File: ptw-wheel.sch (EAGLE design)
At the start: 3 parts

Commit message: Create board data
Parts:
- removed ARDUINO_NANO3: Arduino Nano, ArduinoNanoV30:ARDUINO_NANO
- removed KNS1: KONASHI-2.0, konashi-2.0:KONASHI-2.0
- added ARDUINO_NANO1: (no value), arduinoNanoV30-withoud_drill_hole:ARDUINO_NANO
- added U$1: KONASHI2.0, konashiv2-withoud_drill_hole:KONASHI2.0
- added USB1: USBCON, usbcon:USBCON
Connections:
- removed net N$2: ARDUINO_NANO3.GND@2, JP1.3
- removed net N$6: ARDUINO_NANO3.GND@1, KNS1.UART-GND
- new net +5V: ARDUINO_NANO1.5V, JP1.1, U$1.+5V, USB1.5V
- new net GND: ARDUINO_NANO1.GND@1, JP1.3, U$1.GND, U$1.GND@1, U$1.GND@2, USB1.GND, USB1.SHIELD
- net N$1: now also ARDUINO_NANO1.GND@2, U$1.GND@3; no longer ARDUINO_NANO3.5V, JP1.1, KNS1.+5V
- net N$3: now also ARDUINO_NANO1.D6/AIN0; no longer ARDUINO_NANO3.D6/AIN0
- net N$4: now also ARDUINO_NANO1.D0/RX, U$1.TX; no longer ARDUINO_NANO3.D0/RX, KNS1.UART-TX
- net N$5: now also ARDUINO_NANO1.D1/TX, U$1.RX; no longer ARDUINO_NANO3.D1/TX, KNS1.UART-RX
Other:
- moved on the sheet: JP1

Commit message: Rename connection to 'GND'
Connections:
- removed net N$1: ARDUINO_NANO1.GND@2, U$1.GND@3
- net GND: now also ARDUINO_NANO1.GND@2, U$1.GND@3
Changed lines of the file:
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@@
 <pinref part="U$1" gate="G$1" pin="GND"/>
+</segment>
+<segment>
+<pinref part="ARDUINO_NANO1" gate="G$1" pin="GND@2"/>
+<wire x1="48.26" y1="53.34" x2="53.34" y2="53.34" width="0.1524" layer="91"/>
+<pinref part="SUPPLY5" gate="GND" pin="GND"/>
+<wire x1="53.34" y1="53.34" x2="53.34" y2="40.64" width="0.1524" layer="91"/>
+<pinref part="U$1" gate="G$1" pin="GND@3"/>
+<wire x1="60.96" y1="40.64" x2="53.34" y2="40.64" width="0.1524" layer="91"/>
+<junction x="53.34" y="40.64"/>
 </segment>
 </net>
@@
 </segment>
 </net>
-<net name="N$1" class="0">
-<segment>
-<pinref part="ARDUINO_NANO1" gate="G$1" pin="GND@2"/>
-<wire x1="48.26" y1="53.34" x2="53.34" y2="53.34" width="0.1524" layer="91"/>
-<pinref part="SUPPLY5" gate="GND" pin="GND"/>
-<wire x1="53.34" y1="53.34" x2="53.34" y2="40.64" width="0.1524" layer="91"/>
-<wire x1="60.96" y1="40.64" x2="53.34" y2="40.64" width="0.1524" layer="91"/>
-<junction x="53.34" y="40.64"/>
-<pinref part="U$1" gate="G$1" pin="GND@3"/>
-</segment>
-</net>

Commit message: 更新
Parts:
- renumbered U$1 to KONASHI
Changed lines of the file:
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@@
 <part name="SUPPLY8" library="supply2" library_urn="urn:adsk.eagle:library:372" deviceset="GND" device=""/>
 <part name="SUPPLY10" library="supply2" library_urn="urn:adsk.eagle:library:372" deviceset="GND" device=""/>
-<part name="U$1" library="konashiv2-withoud_drill_hole" deviceset="KONASHI2.0" device=""/>
+<part name="KONASHI" library="konashiv2-withoud_drill_hole" deviceset="KONASHI2.0" device=""/>
 </parts>
 <sheets>
@@
 <attribute name="VALUE" x="104.775" y="14.605" size="1.778" layer="96"/>
 </instance>
-<instance part="U$1" gate="G$1" x="83.82" y="33.02" smashed="yes" rot="R90"/>
+<instance part="KONASHI" gate="G$1" x="83.82" y="33.02" smashed="yes" rot="R90"/>
 </instances>
 <busses>
@@
 <wire x1="58.42" y1="43.18" x2="60.96" y2="43.18" width="0.1524" layer="91"/>
 <pinref part="ARDUINO_NANO1" gate="G$1" pin="D0/RX"/>
-<pinref part="U$1" gate="G$1" pin="TX"/>
+<pinref part="KONASHI" gate="G$1" pin="TX"/>
 </segment>
 </net>
@@
 <wire x1="55.88" y1="38.1" x2="60.96" y2="38.1" width="0.1524" layer="91"/>
 <pinref part="ARDUINO_NANO1" gate="G$1" pin="D1/TX"/>
-<pinref part="U$1" gate="G$1" pin="RX"/>
+<pinref part="KONASHI" gate="G$1" pin="RX"/>
 </segment>
 </net>
@@
 <wire x1="106.68" y1="35.56" x2="111.76" y2="35.56" width="0.1524" layer="91"/>
 <pinref part="SUPPLY2" gate="GND" pin="GND"/>
-<pinref part="U$1" gate="G$1" pin="GND@1"/>
+<pinref part="KONASHI" gate="G$1" pin="GND@1"/>
 </segment>
 <segment>
@@
 <segment>
 <pinref part="SUPPLY8" gate="GND" pin="GND"/>
-<pinref part="U$1" gate="G$1" pin="GND@2"/>
+<pinref part="KONASHI" gate="G$1" pin="GND@2"/>
 </segment>
 <segment>
 <pinref part="SUPPLY10" gate="GND" pin="GND"/>
-<pinref part="U$1" gate="G$1" pin="GND"/>
+<pinref part="KONASHI" gate="G$1" pin="GND"/>
 </segment>
 <segment>
@@
 <pinref part="SUPPLY5" gate="GND" pin="GND"/>
 <wire x1="53.34" y1="53.34" x2="53.34" y2="40.64" width="0.1524" layer="91"/>
-<pinref part="U$1" gate="G$1" pin="GND@3"/>
+<pinref part="KONASHI" gate="G$1" pin="GND@3"/>
 <wire x1="60.96" y1="40.64" x2="53.34" y2="40.64" width="0.1524" layer="91"/>
 <junction x="53.34" y="40.64"/>
@@
 <pinref part="SUPPLY9" gate="+5V" pin="+5V"/>
 <junction x="111.76" y="40.64"/>
-<pinref part="U$1" gate="G$1" pin="+5V"/>
+<pinref part="KONASHI" gate="G$1" pin="+5V"/>
 </segment>
 <segment>

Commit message: ボードのレイアウト整理
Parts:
- renumbered ARDUINO_NANO1 to ARDUINO_NANO, USB1 to USB
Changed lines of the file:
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@@
 <parts>
 <part name="JP1" library="pinhead" library_urn="urn:adsk.eagle:library:325" deviceset="PINHD-1X3" device="" package3d_urn="urn:adsk.eagle:package:22458/2" value="LED tapes"/>
-<part name="USB1" library="usbcon" deviceset="USBCON" device=""/>
-<part name="ARDUINO_NANO1" library="arduinoNanoV30-withoud_drill_hole" deviceset="ARDUINO_NANO" device=""/>
+<part name="USB" library="usbcon" deviceset="USBCON" device=""/>
+<part name="ARDUINO_NANO" library="arduinoNanoV30-withoud_drill_hole" deviceset="ARDUINO_NANO" device=""/>
 <part name="SUPPLY1" library="supply2" library_urn="urn:adsk.eagle:library:372" deviceset="GND" device=""/>
 <part name="SUPPLY2" library="supply2" library_urn="urn:adsk.eagle:library:372" deviceset="GND" device=""/>
@@
 <attribute name="VALUE" x="129.54" y="57.15" size="1.778" layer="96" rot="R180"/>
 </instance>
-<instance part="USB1" gate="G$1" x="83.82" y="60.96" smashed="yes">
+<instance part="USB" gate="G$1" x="83.82" y="60.96" smashed="yes">
 <attribute name="NAME" x="78.74" y="68.58" size="1.778" layer="95"/>
 <attribute name="VALUE" x="78.74" y="50.8" size="1.778" layer="96"/>
 </instance>
-<instance part="ARDUINO_NANO1" gate="G$1" x="27.94" y="33.02" smashed="yes">
+<instance part="ARDUINO_NANO" gate="G$1" x="27.94" y="33.02" smashed="yes">
 <attribute name="NAME" x="12.7" y="12.7" size="1.778" layer="95"/>
 <attribute name="VALUE" x="12.7" y="10.16" size="1.778" layer="96"/>
@@
 <wire x1="7.62" y1="35.56" x2="5.08" y2="35.56" width="0.1524" layer="91"/>
 <wire x1="5.08" y1="35.56" x2="5.08" y2="7.62" width="0.1524" layer="91"/>
-<pinref part="ARDUINO_NANO1" gate="G$1" pin="D6/AIN0"/>
+<pinref part="ARDUINO_NANO" gate="G$1" pin="D6/AIN0"/>
 </segment>
 </net>
@@
 <wire x1="58.42" y1="63.5" x2="58.42" y2="43.18" width="0.1524" layer="91"/>
 <wire x1="58.42" y1="43.18" x2="60.96" y2="43.18" width="0.1524" layer="91"/>
-<pinref part="ARDUINO_NANO1" gate="G$1" pin="D0/RX"/>
+<pinref part="ARDUINO_NANO" gate="G$1" pin="D0/RX"/>
 <pinref part="KONASHI" gate="G$1" pin="TX"/>
 </segment>
@@
 <wire x1="55.88" y1="66.04" x2="55.88" y2="38.1" width="0.1524" layer="91"/>
 <wire x1="55.88" y1="38.1" x2="60.96" y2="38.1" width="0.1524" layer="91"/>
-<pinref part="ARDUINO_NANO1" gate="G$1" pin="D1/TX"/>
+<pinref part="ARDUINO_NANO" gate="G$1" pin="D1/TX"/>
 <pinref part="KONASHI" gate="G$1" pin="RX"/>
 </segment>
@@
 <net name="GND" class="0">
 <segment>
-<pinref part="USB1" gate="G$1" pin="GND"/>
+<pinref part="USB" gate="G$1" pin="GND"/>
 <wire x1="83.82" y1="60.96" x2="73.66" y2="60.96" width="0.1524" layer="91"/>
 <wire x1="73.66" y1="60.96" x2="73.66" y2="58.42" width="0.1524" layer="91"/>
-<pinref part="USB1" gate="G$1" pin="SHIELD"/>
+<pinref part="USB" gate="G$1" pin="SHIELD"/>
 <wire x1="83.82" y1="58.42" x2="73.66" y2="58.42" width="0.1524" layer="91"/>
 <junction x="73.66" y="58.42"/>
@@
 </segment>
 <segment>
-<pinref part="ARDUINO_NANO1" gate="G$1" pin="GND@1"/>
+<pinref part="ARDUINO_NANO" gate="G$1" pin="GND@1"/>
 <pinref part="SUPPLY4" gate="GND" pin="GND"/>
 <wire x1="2.54" y1="48.26" x2="7.62" y2="48.26" width="0.1524" layer="91"/>
@@
 </segment>
 <segment>
-<pinref part="ARDUINO_NANO1" gate="G$1" pin="GND@2"/>
+<pinref part="ARDUINO_NANO" gate="G$1" pin="GND@2"/>
 <wire x1="48.26" y1="53.34" x2="53.34" y2="53.34" width="0.1524" layer="91"/>
 <pinref part="SUPPLY5" gate="GND" pin="GND"/>
@@
 <net name="+5V" class="0">
 <segment>
-<pinref part="USB1" gate="G$1" pin="5V"/>
+<pinref part="USB" gate="G$1" pin="5V"/>
 <wire x1="83.82" y1="63.5" x2="73.66" y2="63.5" width="0.1524" layer="91"/>
 <pinref part="SUPPLY6" gate="+5V" pin="+5V"/>
@@
 <segment>
 <wire x1="48.26" y1="48.26" x2="50.8" y2="48.26" width="0.1524" layer="91"/>
-<pinref part="ARDUINO_NANO1" gate="G$1" pin="5V"/>
+<pinref part="ARDUINO_NANO" gate="G$1" pin="5V"/>
 <pinref part="SUPPLY7" gate="+5V" pin="+5V"/>
 </segment>

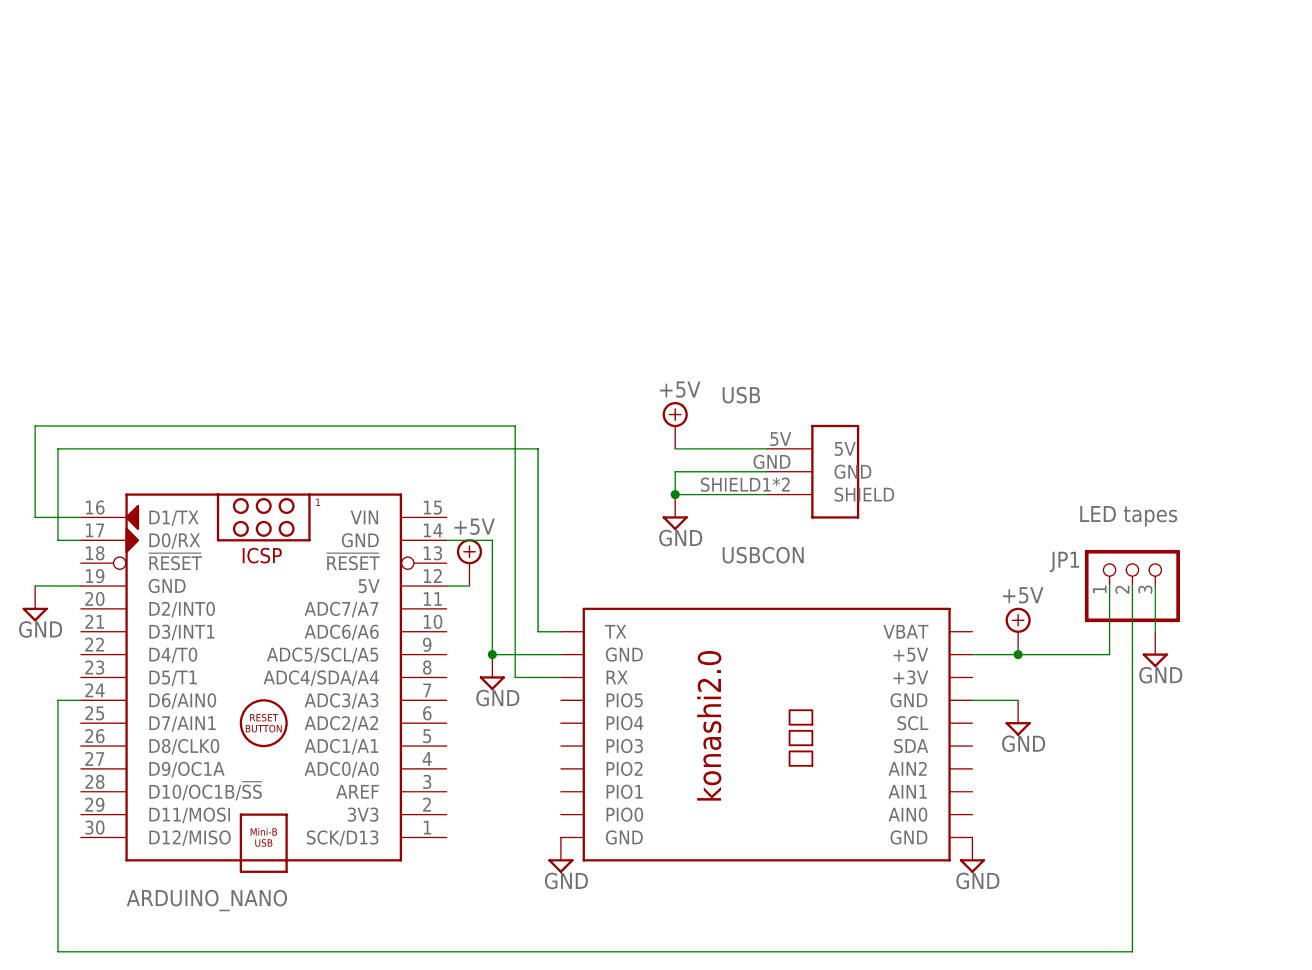
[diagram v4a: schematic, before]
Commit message: トグルスイッチを追加
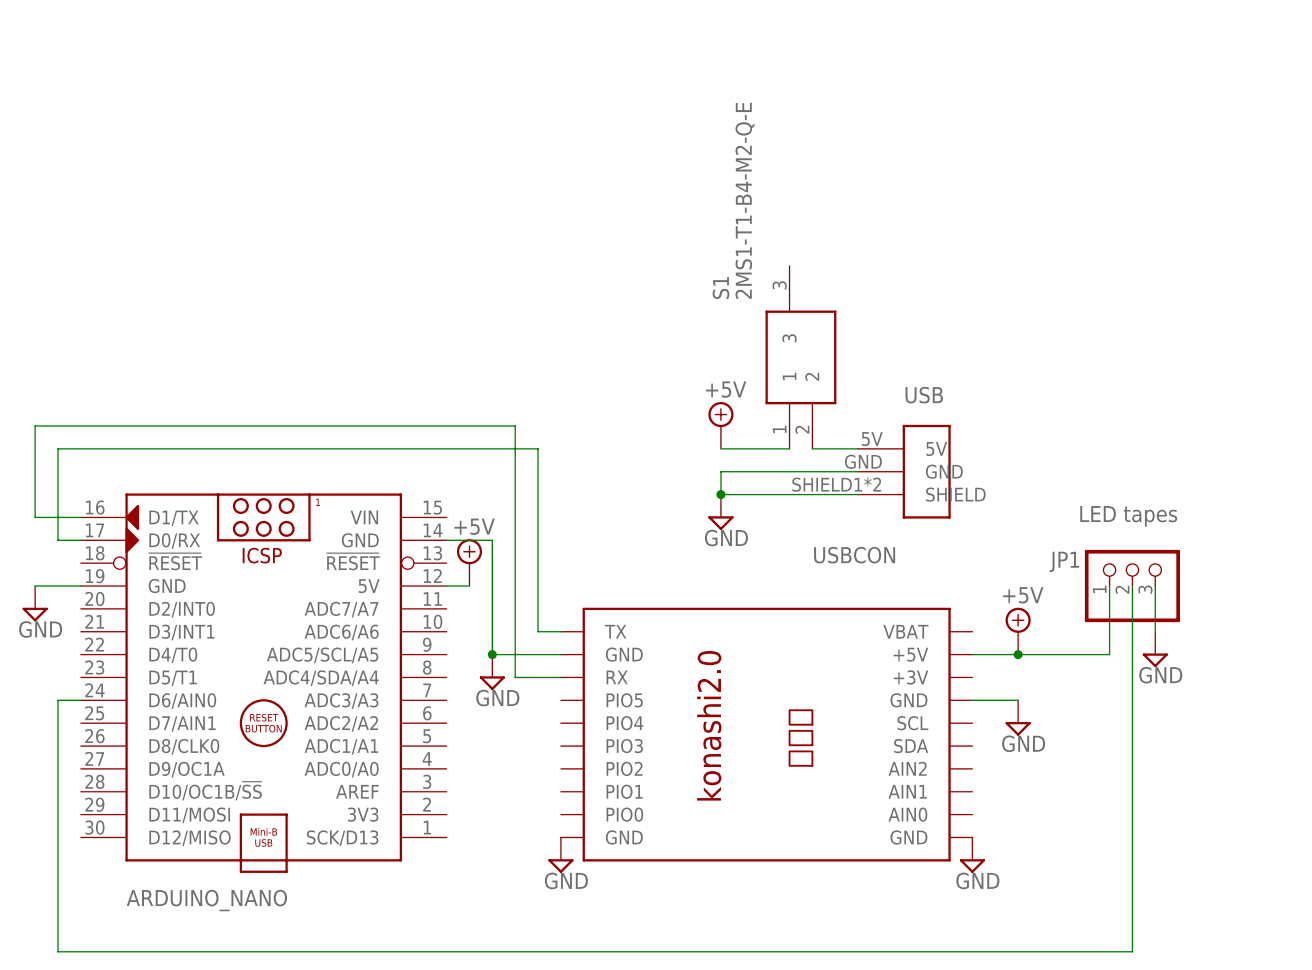
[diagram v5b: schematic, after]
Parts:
- added S1: 2MS1-T1-B4-M2-Q-E, 2MS1-T1-B4-VS2-Q-E:2MS1-T1-B4-M2-Q-E
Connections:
- new net N$1: S1.2, USB.5V
- net +5V: now also S1.1; no longer USB.5V
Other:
- moved on the sheet: USB
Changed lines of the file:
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@@
 <part name="SUPPLY10" library="supply2" library_urn="urn:adsk.eagle:library:372" deviceset="GND" device=""/>
 <part name="KONASHI" library="konashiv2-withoud_drill_hole" deviceset="KONASHI2.0" device=""/>
+<part name="S1" library="2MS1-T1-B4-VS2-Q-E" deviceset="2MS1-T1-B4-M2-Q-E" device=""/>
 </parts>
 <sheets>
@@
 <attribute name="VALUE" x="129.54" y="57.15" size="1.778" layer="96" rot="R180"/>
 </instance>
-<instance part="USB" gate="G$1" x="83.82" y="60.96" smashed="yes">
-<attribute name="NAME" x="78.74" y="68.58" size="1.778" layer="95"/>
-<attribute name="VALUE" x="78.74" y="50.8" size="1.778" layer="96"/>
+<instance part="USB" gate="G$1" x="93.98" y="60.96" smashed="yes">
+<attribute name="NAME" x="99.06" y="68.58" size="1.778" layer="95"/>
+<attribute name="VALUE" x="88.9" y="50.8" size="1.778" layer="96"/>
 </instance>
 <instance part="ARDUINO_NANO" gate="G$1" x="27.94" y="33.02" smashed="yes">
@@
 <attribute name="VALUE" x="12.7" y="10.16" size="1.778" layer="96"/>
 </instance>
-<instance part="SUPPLY1" gate="GND" x="73.66" y="55.88" smashed="yes">
-<attribute name="VALUE" x="71.755" y="52.705" size="1.778" layer="96"/>
+<instance part="SUPPLY1" gate="GND" x="78.74" y="55.88" smashed="yes">
+<attribute name="VALUE" x="76.835" y="52.705" size="1.778" layer="96"/>
 </instance>
 <instance part="SUPPLY2" gate="GND" x="111.76" y="33.02" smashed="yes">
@@
 <attribute name="VALUE" x="51.435" y="34.925" size="1.778" layer="96"/>
 </instance>
-<instance part="SUPPLY6" gate="+5V" x="73.66" y="66.04" smashed="yes">
-<attribute name="VALUE" x="71.755" y="69.215" size="1.778" layer="96"/>
+<instance part="SUPPLY6" gate="+5V" x="78.74" y="66.04" smashed="yes">
+<attribute name="VALUE" x="76.835" y="69.215" size="1.778" layer="96"/>
 </instance>
 <instance part="SUPPLY9" gate="+5V" x="111.76" y="43.18" smashed="yes">
@@
 </instance>
 <instance part="KONASHI" gate="G$1" x="83.82" y="33.02" smashed="yes" rot="R90"/>
+<instance part="S1" gate="G$1" x="86.36" y="63.5" smashed="yes" rot="R90">
+<attribute name="NAME" x="78.74" y="80.01" size="1.778" layer="95" rot="R90" align="center-left"/>
+<attribute name="VALUE" x="81.28" y="80.01" size="1.778" layer="96" rot="R90" align="center-left"/>
+</instance>
 </instances>
 <busses>
@@
 <segment>
 <pinref part="USB" gate="G$1" pin="GND"/>
-<wire x1="83.82" y1="60.96" x2="73.66" y2="60.96" width="0.1524" layer="91"/>
-<wire x1="73.66" y1="60.96" x2="73.66" y2="58.42" width="0.1524" layer="91"/>
+<wire x1="93.98" y1="60.96" x2="78.74" y2="60.96" width="0.1524" layer="91"/>
+<wire x1="78.74" y1="60.96" x2="78.74" y2="58.42" width="0.1524" layer="91"/>
 <pinref part="USB" gate="G$1" pin="SHIELD"/>
-<wire x1="83.82" y1="58.42" x2="73.66" y2="58.42" width="0.1524" layer="91"/>
-<junction x="73.66" y="58.42"/>
+<wire x1="93.98" y1="58.42" x2="78.74" y2="58.42" width="0.1524" layer="91"/>
+<junction x="78.74" y="58.42"/>
 <pinref part="SUPPLY1" gate="GND" pin="GND"/>
 </segment>
@@
 <net name="+5V" class="0">
 <segment>
-<pinref part="USB" gate="G$1" pin="5V"/>
-<wire x1="83.82" y1="63.5" x2="73.66" y2="63.5" width="0.1524" layer="91"/>
-<pinref part="SUPPLY6" gate="+5V" pin="+5V"/>
-</segment>
-<segment>
 <pinref part="JP1" gate="A" pin="1"/>
 <wire x1="121.92" y1="48.26" x2="121.92" y2="40.64" width="0.1524" layer="91"/>
@@
 <pinref part="SUPPLY7" gate="+5V" pin="+5V"/>
 </segment>
+<segment>
+<pinref part="S1" gate="G$1" pin="1"/>
+<pinref part="SUPPLY6" gate="+5V" pin="+5V"/>
+<wire x1="78.74" y1="63.5" x2="86.36" y2="63.5" width="0.1524" layer="91"/>
+</segment>
 </net>
+<net name="N$1" class="0">
+<segment>
+<pinref part="USB" gate="G$1" pin="5V"/>
+<pinref part="S1" gate="G$1" pin="2"/>
+<wire x1="93.98" y1="63.5" x2="88.9" y2="63.5" width="0.1524" layer="91"/>
+</segment>
+</net>

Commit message: 調整
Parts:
- ARDUINO_NANO: device arduinoNanoV30-withoud_drill_hole:ARDUINO_NANO -> ArduinoNanoV30:ARDUINO_NANO
- JP1: value LED tapes -> LED tape
- KONASHI: device konashiv2-withoud_drill_hole:KONASHI2.0 -> konashiv2:KONASHI2.0
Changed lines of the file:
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@@
 </classes>
 <parts>
-<part name="JP1" library="pinhead" library_urn="urn:adsk.eagle:library:325" deviceset="PINHD-1X3" device="" package3d_urn="urn:adsk.eagle:package:22458/2" value="LED tapes"/>
+<part name="JP1" library="pinhead" library_urn="urn:adsk.eagle:library:325" deviceset="PINHD-1X3" device="" package3d_urn="urn:adsk.eagle:package:22458/2" value="LED tape"/>
 <part name="USB" library="usbcon" deviceset="USBCON" device=""/>
-<part name="ARDUINO_NANO" library="arduinoNanoV30-withoud_drill_hole" deviceset="ARDUINO_NANO" device=""/>
+<part name="ARDUINO_NANO" library="ArduinoNanoV30" deviceset="ARDUINO_NANO" device=""/>
 <part name="SUPPLY1" library="supply2" library_urn="urn:adsk.eagle:library:372" deviceset="GND" device=""/>
 <part name="SUPPLY2" library="supply2" library_urn="urn:adsk.eagle:library:372" deviceset="GND" device=""/>
@@
 <part name="SUPPLY8" library="supply2" library_urn="urn:adsk.eagle:library:372" deviceset="GND" device=""/>
 <part name="SUPPLY10" library="supply2" library_urn="urn:adsk.eagle:library:372" deviceset="GND" device=""/>
-<part name="KONASHI" library="konashiv2-withoud_drill_hole" deviceset="KONASHI2.0" device=""/>
+<part name="KONASHI" library="konashiv2" deviceset="KONASHI2.0" device=""/>
 <part name="S1" library="2MS1-T1-B4-VS2-Q-E" deviceset="2MS1-T1-B4-M2-Q-E" device=""/>
 </parts>
